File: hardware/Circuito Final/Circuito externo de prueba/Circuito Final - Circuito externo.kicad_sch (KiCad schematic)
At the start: 16 parts, among them J1 Conn_02x19_Odd_Even, J2 Conn_02x19_Odd_Even, J3 Conn_01x02, J4 Conn_01x02, J5 Conn_01x02_Socket, SW1 SW_DIP_x04, SW2 SW_DIP_x04, SW4 SW_DIP_x01, SW5 SW_DIP_x01, SW6 SW_DIP_x01

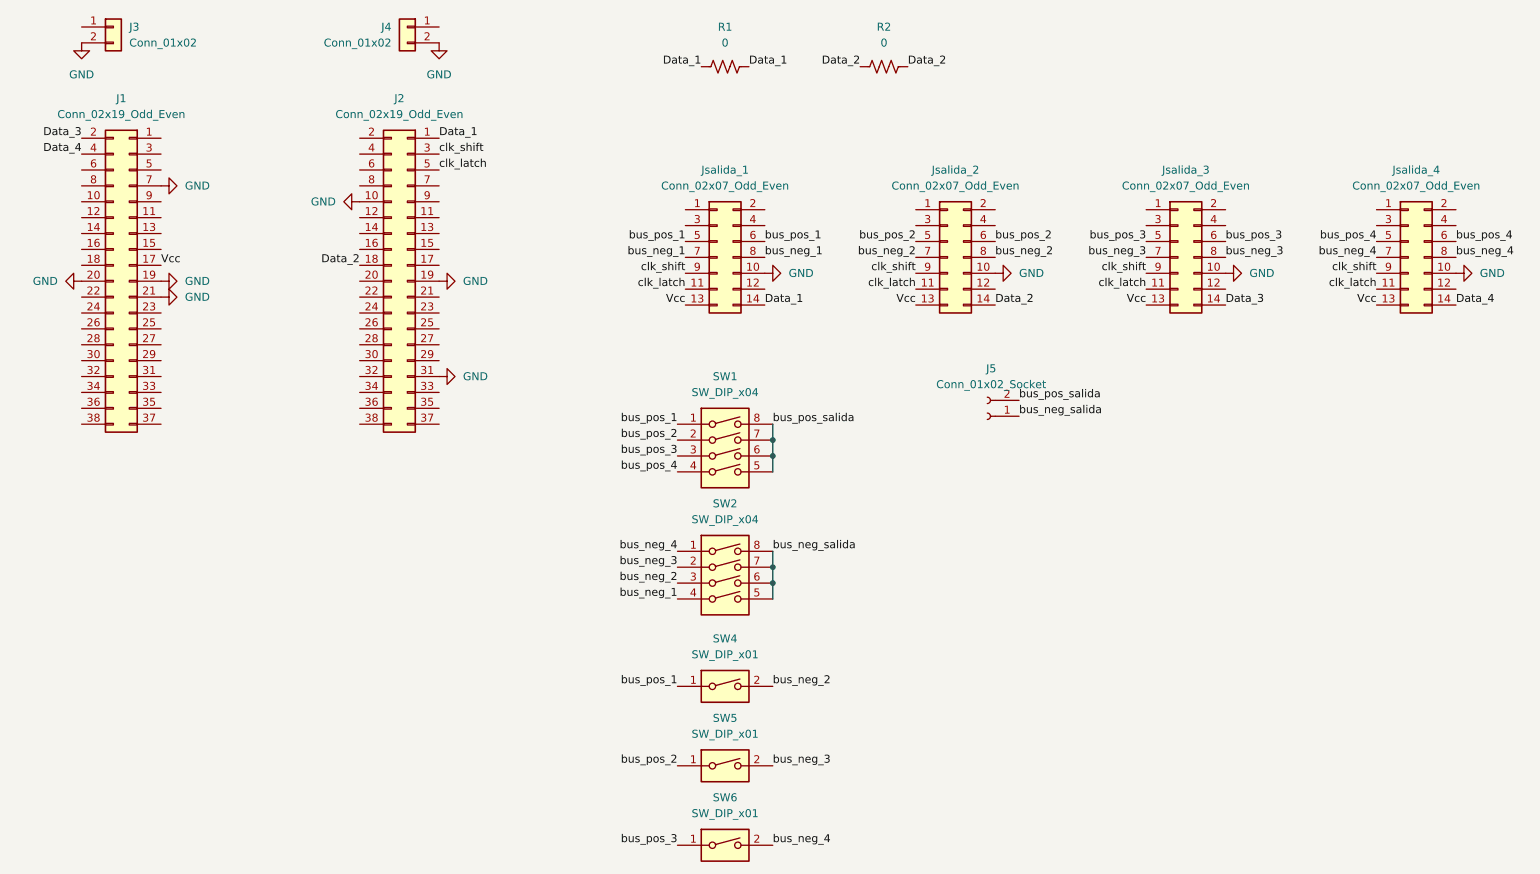
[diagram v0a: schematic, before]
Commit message: subida de mediciones de switcheo con dos bancos, bitacora y kicad del circuito externo de prueba terminado
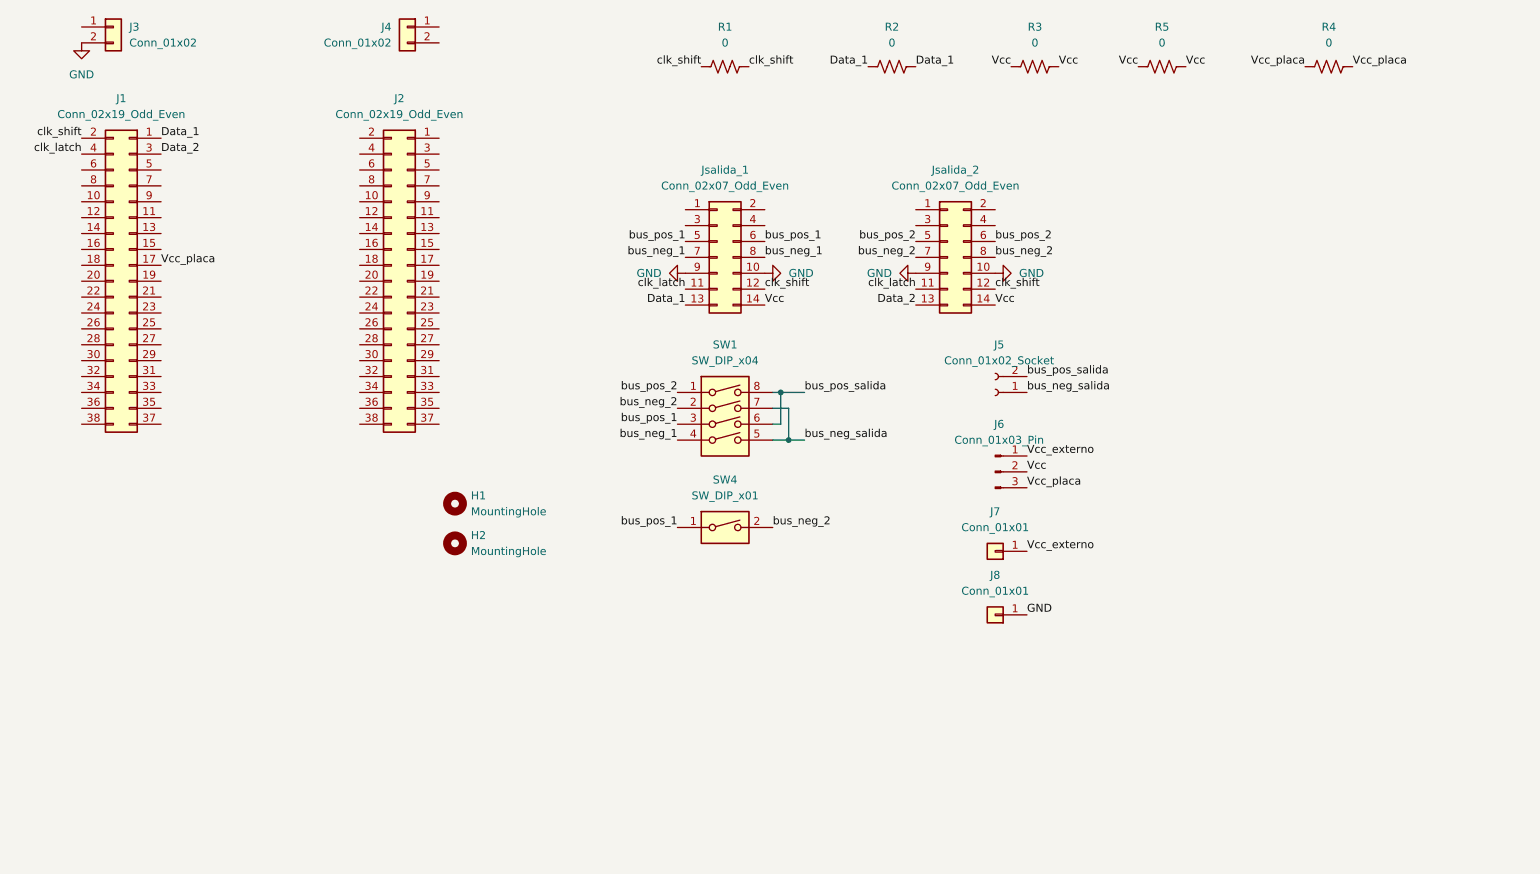
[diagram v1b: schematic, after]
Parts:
- removed Jsalida_3, Jsalida_4: Conn_02x07_Odd_Even, Connector_PinHeader_2.54mm:PinHeader_2x07_P2.54mm_Vertical, symbol Connector_Generic:Conn_02x07_Odd_Even
- removed SW2: SW_DIP_x04, Button_Switch_THT:SW_DIP_SPSTx04_Slide_6.7x11.72mm_W7.62mm_P2.54mm_LowProfile, symbol Switch:SW_DIP_x04
- removed SW5, SW6: SW_DIP_x01, Button_Switch_THT:SW_DIP_SPSTx01_Slide_9.78x4.72mm_W7.62mm_P2.54mm, symbol Switch:SW_DIP_x01
- added H1, H2: MountingHole, MountingHole:MountingHole_3mm, symbol Mechanical:MountingHole
- added J6: Conn_01x03_Pin, Connector_PinHeader_2.54mm:PinHeader_1x03_P2.54mm_Vertical, symbol Connector:Conn_01x03_Pin
- added J7, J8: Conn_01x01, Connector_PinHeader_2.54mm:PinHeader_1x01_P2.54mm_Vertical, symbol Connector_Generic:Conn_01x01
- added R3, R4, R5: 0, Resistor_SMD:R_1206_3216Metric_Pad1.30x1.75mm_HandSolder, symbol Device:R_US
- SW1: footprint Button_Switch_THT:SW_DIP_SPSTx04_Slide_6.7x11.72mm_W7.62mm_P2.54mm_LowProfile -> Button_Switch_THT:SW_DIP_SPSTx04_Slide_9.78x12.34mm_W7.62mm_P2.54mm
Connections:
- net Data_3 is gone; now on net clk_shift: J1.2 (Pin_2)
- net Data_4 is gone; now on net clk_latch: J1.4 (Pin_4)
- net bus_pos_3 is gone; now on net bus_pos_1: SW1.3
- net bus_pos_4 is gone; now on net bus_neg_1: SW1.4
- net Data_1: now also J1.1 (Pin_1), Jsalida_1.13 (Pin_13), R2.1, R2.2; no longer J2.1 (Pin_1), Jsalida_1.14 (Pin_14), R1.1, R1.2
- net Data_2: now also J1.3 (Pin_3), Jsalida_2.13 (Pin_13); no longer J2.18 (Pin_18), Jsalida_2.14 (Pin_14), R2.1, R2.2
- net GND: now also Jsalida_1.9 (Pin_9), Jsalida_2.9 (Pin_9), J8.1 (Pin_1); no longer J1.19 (Pin_19), J1.20 (Pin_20), J1.21 (Pin_21), J1.7 (Pin_7), J2.10 (Pin_10), J2.19 (Pin_19), J2.31 (Pin_31), J4.2 (Pin_2)
- net Vcc: now also Jsalida_1.14 (Pin_14), Jsalida_2.14 (Pin_14), J6.2 (Pin_2), R3.1, R3.2, R5.1, R5.2; no longer J1.17 (Pin_17), Jsalida_1.13 (Pin_13), Jsalida_2.13 (Pin_13)
- net bus_neg_2: now also SW1.2
- net bus_neg_salida: now also SW1.5, SW1.7
- net bus_pos_1: no longer SW1.1
- net bus_pos_2: now also SW1.1; no longer SW1.2
- net bus_pos_salida: no longer SW1.5, SW1.7
- net clk_latch: no longer J2.5 (Pin_5)
- net clk_shift: now also Jsalida_1.12 (Pin_12), Jsalida_2.12 (Pin_12), R1.1, R1.2; no longer J2.3 (Pin_3), Jsalida_1.9 (Pin_9), Jsalida_2.9 (Pin_9)
- new net Vcc_externo: J6.1 (Pin_1), J7.1 (Pin_1)
- new net Vcc_placa: J1.17 (Pin_17), J6.3 (Pin_3), R4.1, R4.2
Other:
- moved on the sheet: J5, SW1, SW4
